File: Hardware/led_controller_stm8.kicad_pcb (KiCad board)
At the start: 2 copper layers, 79.5 x 23 mm, 11 parts, among them J1 WS_LED, J2 PROGRAMMING, J3 EXT_BTN, SW1 SW_Push, U1 STM8S103F3

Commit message: update pcb
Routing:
- net GND: track 121.5 -> 128.0 mm
- net /BTN: track 27.0 -> 33.5 mm

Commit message: add pcb
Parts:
- removed C4: 1uF, Capacitor_SMD:C_0805_2012Metric_Pad1.15x1.40mm_HandSolder
- removed J3: EXT_BTN, Connector_JST:JST_PH_B2B-PH-K_1x02_P2.00mm_Vertical
- added D1: BAV99, Package_TO_SOT_SMD:SOT-23, F.Cu at (148.4, 71.2)
- added Q1: IRLML6401, Package_TO_SOT_SMD:SOT-23, F.Cu at (139.2, 61.8)
- added Q2: IRLML6401, Package_TO_SOT_SMD:SOT-23, F.Cu at (142.0, 68.5)
- added Q3: 2N7002, Package_TO_SOT_SMD:SOT-23, F.Cu at (146.8, 61.8)
- added Q4: MMBT3904, Package_TO_SOT_SMD:SOT-23, F.Cu at (153.5, 61.8)
- added R2: 15k, Resistor_SMD:R_0805_2012Metric_Pad1.15x1.40mm_HandSolder, F.Cu at (148.2, 66.5)
- added R3: 150k, Resistor_SMD:R_0805_2012Metric_Pad1.15x1.40mm_HandSolder, F.Cu at (149.8, 61.8)
- added R4: 150k, Resistor_SMD:R_0805_2012Metric_Pad1.15x1.40mm_HandSolder, F.Cu at (138.2, 66.5)
- added R5: 100, Resistor_SMD:R_0805_2012Metric_Pad1.15x1.40mm_HandSolder, F.Cu at (152.5, 68.5)
- added R6: 150k, Resistor_SMD:R_0805_2012Metric_Pad1.15x1.40mm_HandSolder, F.Cu at (145.2, 72.5)
- added R7: 470, Resistor_SMD:R_0805_2012Metric_Pad1.15x1.40mm_HandSolder, F.Cu at (173.5, 65.5)
- C3: value 1nF -> 1uF
- J1: value WS_LED -> PROGRAMMING; footprint Connector_JST:JST_PH_B3B-PH-K_1x03_P2.00mm_Vertical -> local:IDC-1.27-6P
- J2: value PROGRAMMING -> WS_LED; footprint local:IDC-1.27-6P -> Connector_JST:JST_XH_B3B-XH-A_1x03_P2.50mm_Vertical
- R1: value 12k -> 150k
- moved J1 58.8 mm to (132.0, 66.2)
- moved J2 56.1 mm to (193.0, 62.5), turned to 270 degrees
- moved SW1 16.4 mm to (185.7, 67.2)
- moved R1 15.3 mm to (142.0, 65.5), turned to 0 degrees
- moved U1 14.1 mm to (166.6, 65.2)
- moved C2 12.5 mm to (158.8, 68.5), turned to 90 degrees
- moved C1 10.5 mm to (156.6, 68.5), turned to 90 degrees
- moved C3 3.55 mm to (161.0, 65.5)
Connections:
- BT1 pad 1: +BATT -> Net-(BT1-Pad1)
- C3 pad 1: GND -> Net-(C3-Pad1)
- C3 pad 2: /BTN -> GND
- J1 pad 1: GND -> (no net)
- J1 pad 2: +BATT -> GND
- J1 pad 3: /WS_LED -> /NRST
- J2 pad 1: (no net) -> +BATT
- J2 pad 2: GND -> Net-(J2-Pad2)
- J2 pad 3: /NRST -> GND
- R1 pad 1: +BATT -> Net-(Q1-Pad2)
- R1 pad 2: /BTN -> Net-(Q2-Pad1)
- SW1 pad 1: /BTN -> GND
- SW1 pad 2: GND -> Net-(Q2-Pad1)
- U1 pad 1: (no net) -> /PWR_EN
- U1 pad 10: /BTN -> (no net)
- U1 pad 12: (no net) -> /BTN
- U1 pad 19: (no net) -> /BAT_ADC_2
- U1 pad 20: (no net) -> /BAT_ADC_1
- U1 pad 8: Net-(C4-Pad1) -> Net-(C3-Pad1)
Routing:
- net Net-(Q2-Pad1): track 0.00 -> 52.1 mm
- net /BAT_ADC_2: track 0.00 -> 40.7 mm, vias 0 -> 2
- net /WS_LED: track 38.8 -> 4.16 mm
- net /BAT_ADC_1: track 0.00 -> 33.5 mm, vias 0 -> 2
- net +BATT: track 119.7 -> 88.3 mm, vias 0 -> 4
- net /SWIM: track 23.9 -> 45.8 mm, vias 0 -> 1
- net /MCU_RX: track 20.2 -> 41.4 mm, vias 0 -> 1
- net /MCU_TX: track 16.0 -> 36.3 mm, vias 0 -> 1
- net Net-(J2-Pad2): track 0.00 -> 19.7 mm
- net /NRST: track 12.8 -> 31.6 mm, vias 0 -> 1
- net /PWR_EN: track 0.00 -> 17.0 mm
- net Net-(BT1-Pad1): track 0.00 -> 13.9 mm
- net Net-(Q4-Pad2): track 0.00 -> 7.99 mm, vias 0 -> 2
- net GND: track 128.0 -> 133.0 mm
- net Net-(Q3-Pad2): track 0.00 -> 4.81 mm
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- added copper zone on B.Cu, net +BATT
- added copper zone on F.Cu, net +BATT
- added copper zone on F.Cu, net Net-(BT1-Pad1)
- added copper zone on F.Cu, net Net-(Q1-Pad2)

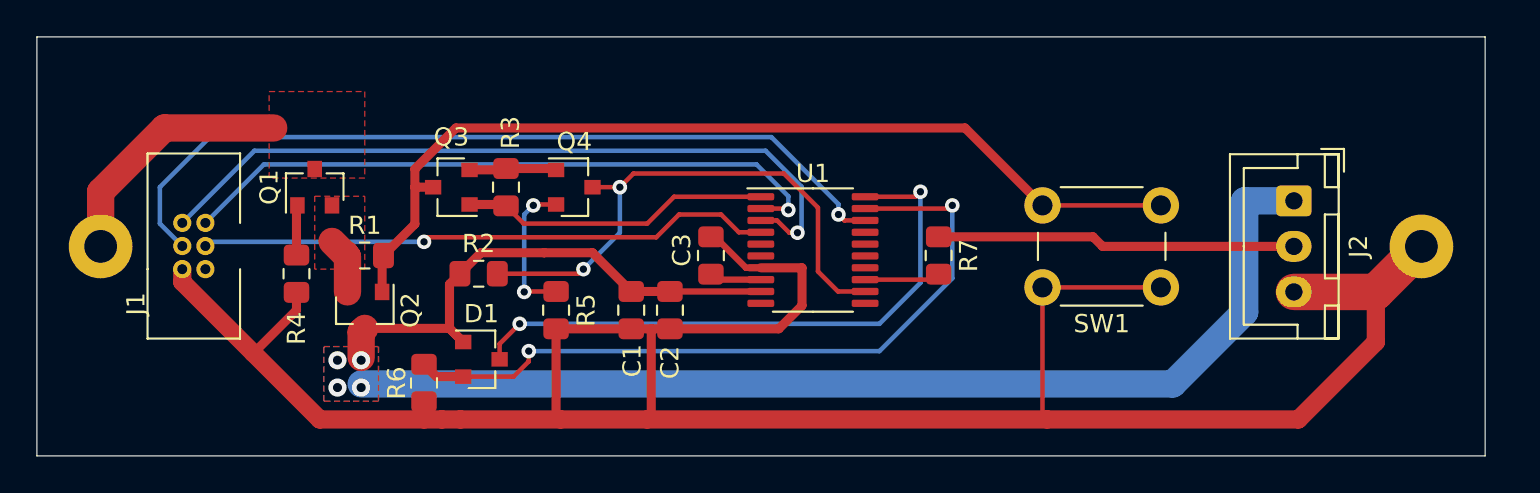
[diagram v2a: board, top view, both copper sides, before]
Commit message: add mounting holes to CB_18650_PC2; update pcb
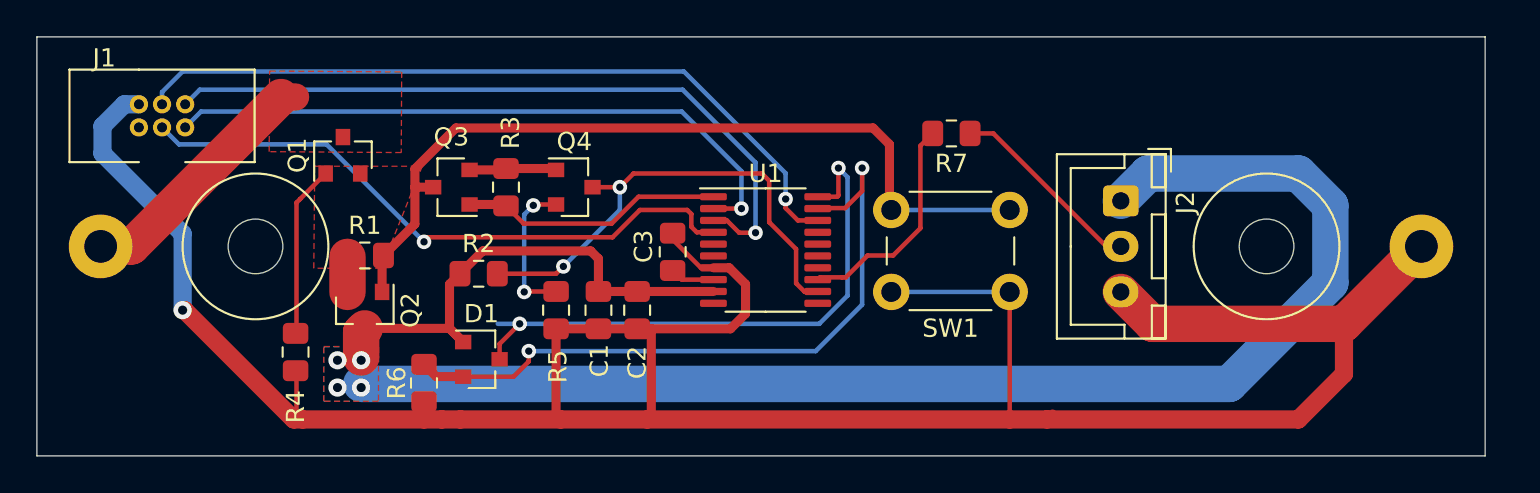
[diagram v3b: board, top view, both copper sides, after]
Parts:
- moved J2 9.50 mm to (183.5, 62.5)
- moved J1 9.36 mm to (129.6, 57.2), turned to 0 degrees
- moved SW1 8.30 mm to (177.4, 67.5)
- moved R7 6.74 mm to (174.2, 58.8), turned to 180 degrees
- moved R4 4.30 mm to (138.2, 70.8)
- moved U1 2.60 mm to (164.0, 65.2)
- moved Q1 2.34 mm to (140.8, 60.0)
- moved C3 2.11 mm to (158.9, 65.3)
- moved C1 1.80 mm to (154.8, 68.5)
- moved C2 1.80 mm to (156.9, 68.5)
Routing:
- net GND: track 133.0 -> 152.1 mm, vias 0 -> 1
- net +BATT: track 88.3 -> 100.4 mm
- net Net-(J2-Pad2): track 19.7 -> 10.8 mm
- net /WS_LED: track 4.16 -> 12.3 mm
- net Net-(Q1-Pad1): track 2.67 -> 9.46 mm
- net Net-(Q2-Pad1): track 52.1 -> 46.0 mm
- net /SWIM: track 45.8 -> 41.6 mm
- net /NRST: track 31.6 -> 34.7 mm
- net /BTN: track 30.2 -> 27.2 mm
- net /BAT_ADC_2: track 40.7 -> 37.9 mm
- net /PWR_EN: track 17.0 -> 14.4 mm
- net /MCU_RX: track 41.4 -> 39.7 mm
- net /BAT_ADC_1: track 33.5 -> 32.1 mm
- net Net-(Q1-Pad2): track 3.13 -> 2.18 mm
- net /MCU_TX: track 36.3 -> 35.8 mm

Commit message: add second horizontal led connector
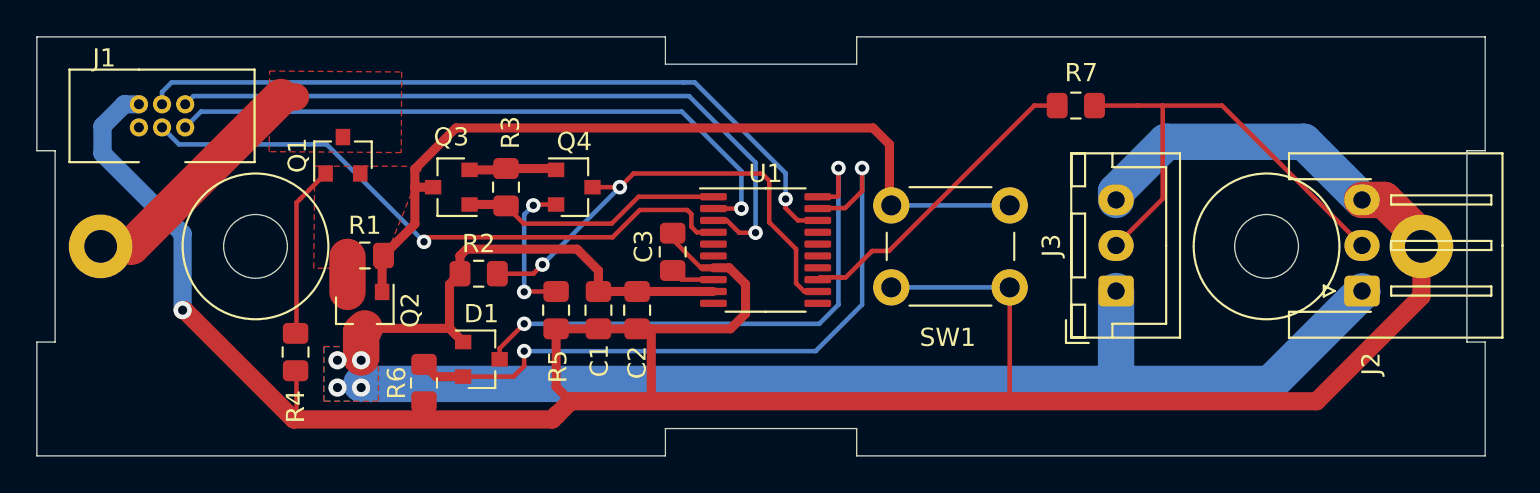
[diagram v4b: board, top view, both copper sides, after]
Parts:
- added J3: WS_LED, Connector_JST:JST_XH_B3B-XH-A_1x03_P2.50mm_Vertical, F.Cu at (183.2, 67.5)
- J2: footprint Connector_JST:JST_XH_B3B-XH-A_1x03_P2.50mm_Vertical -> Connector_JST:JST_XH_S3B-XH-A-1_1x03_P2.50mm_Horizontal
- moved J2 14.1 mm to (196.7, 67.5), turned to 90 degrees
- moved R7 7.00 mm to (181.0, 57.3)
- moved SW1 0.25 mm to (177.4, 67.2)
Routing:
- net Net-(J2-Pad2): track 10.8 -> 26.7 mm
- net +BATT: track 100.4 -> 90.3 mm
- net /WS_LED: track 12.3 -> 17.1 mm
- net GND: track 152.1 -> 154.4 mm
- net /BAT_ADC_1: track 32.1 -> 30.4 mm
- net /BTN: track 27.2 -> 26.5 mm
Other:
- outline, holes or cut-outs redrawn

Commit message: add idc connector legend; add board name
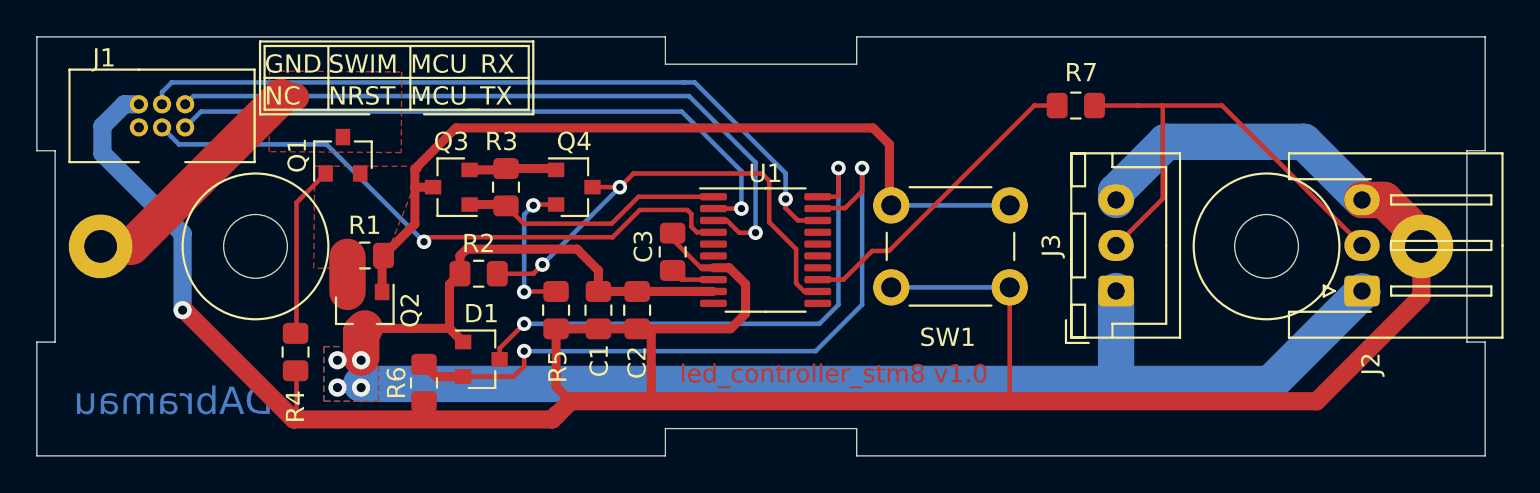
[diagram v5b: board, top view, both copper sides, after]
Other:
- board text added: "DAbramau"
- board text added: "GND"
- board text added: "JLCJLCJLCJLC"
- board text added: "MCU_RX"
- board text added: "MCU_TX"
- board text added: "NC"
- board text added: "NRST"
- board text added: "SWIM"
- board text added: "led_controller_stm8 v1.0"
